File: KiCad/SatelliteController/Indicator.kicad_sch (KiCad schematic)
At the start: 36 parts

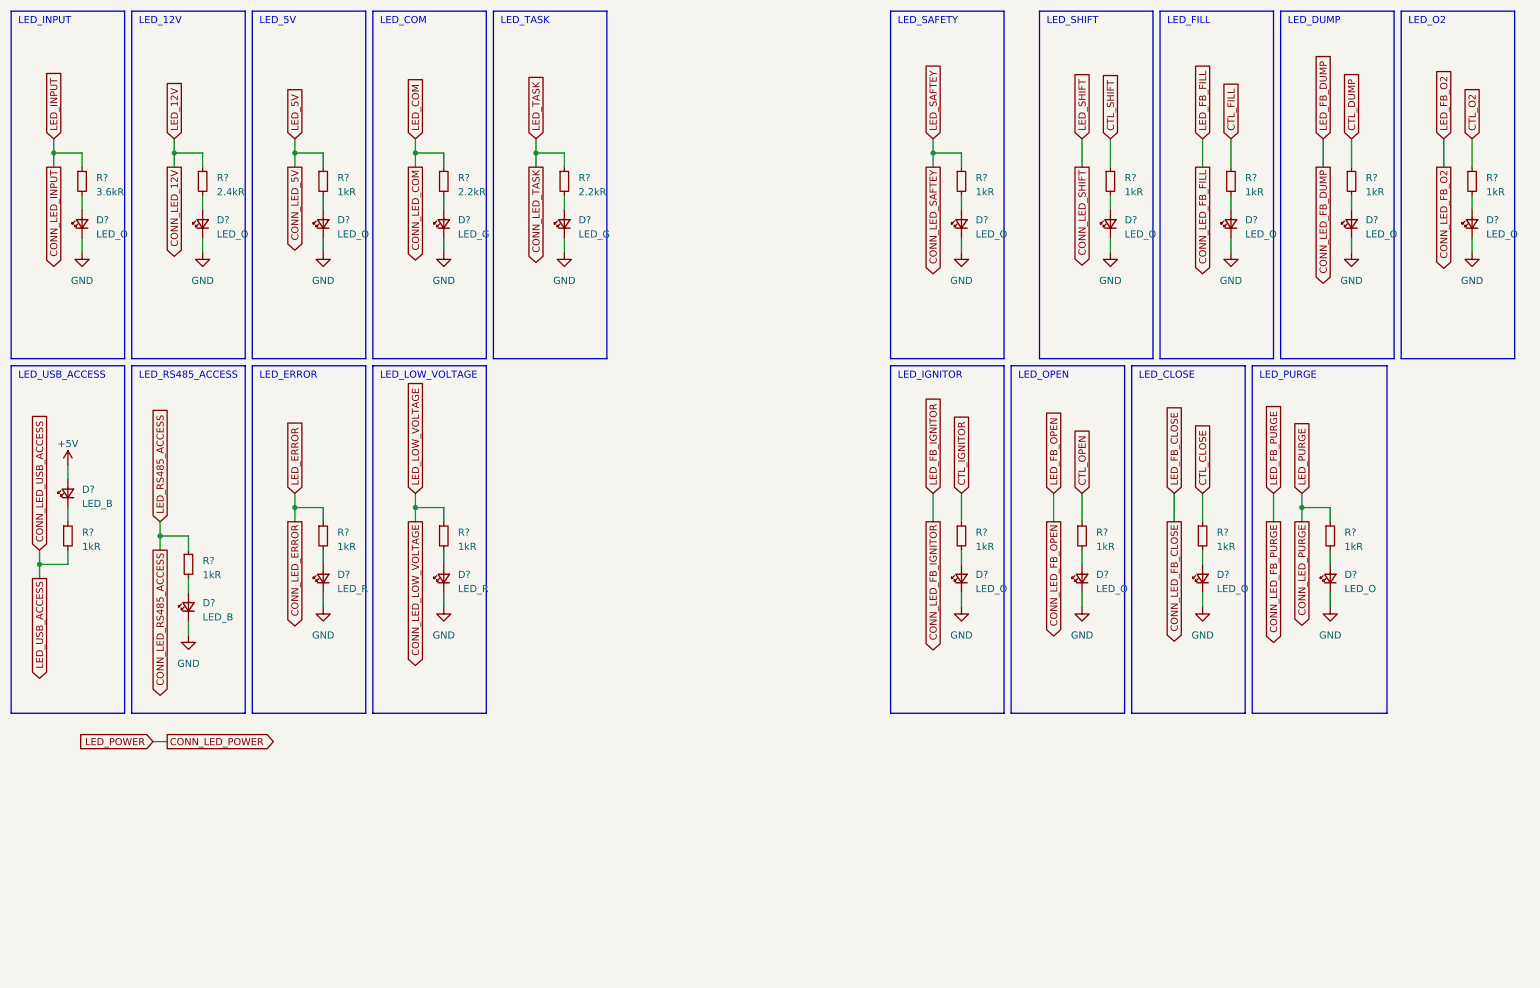
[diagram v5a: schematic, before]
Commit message: サテコンのクリスマスツリーを削除
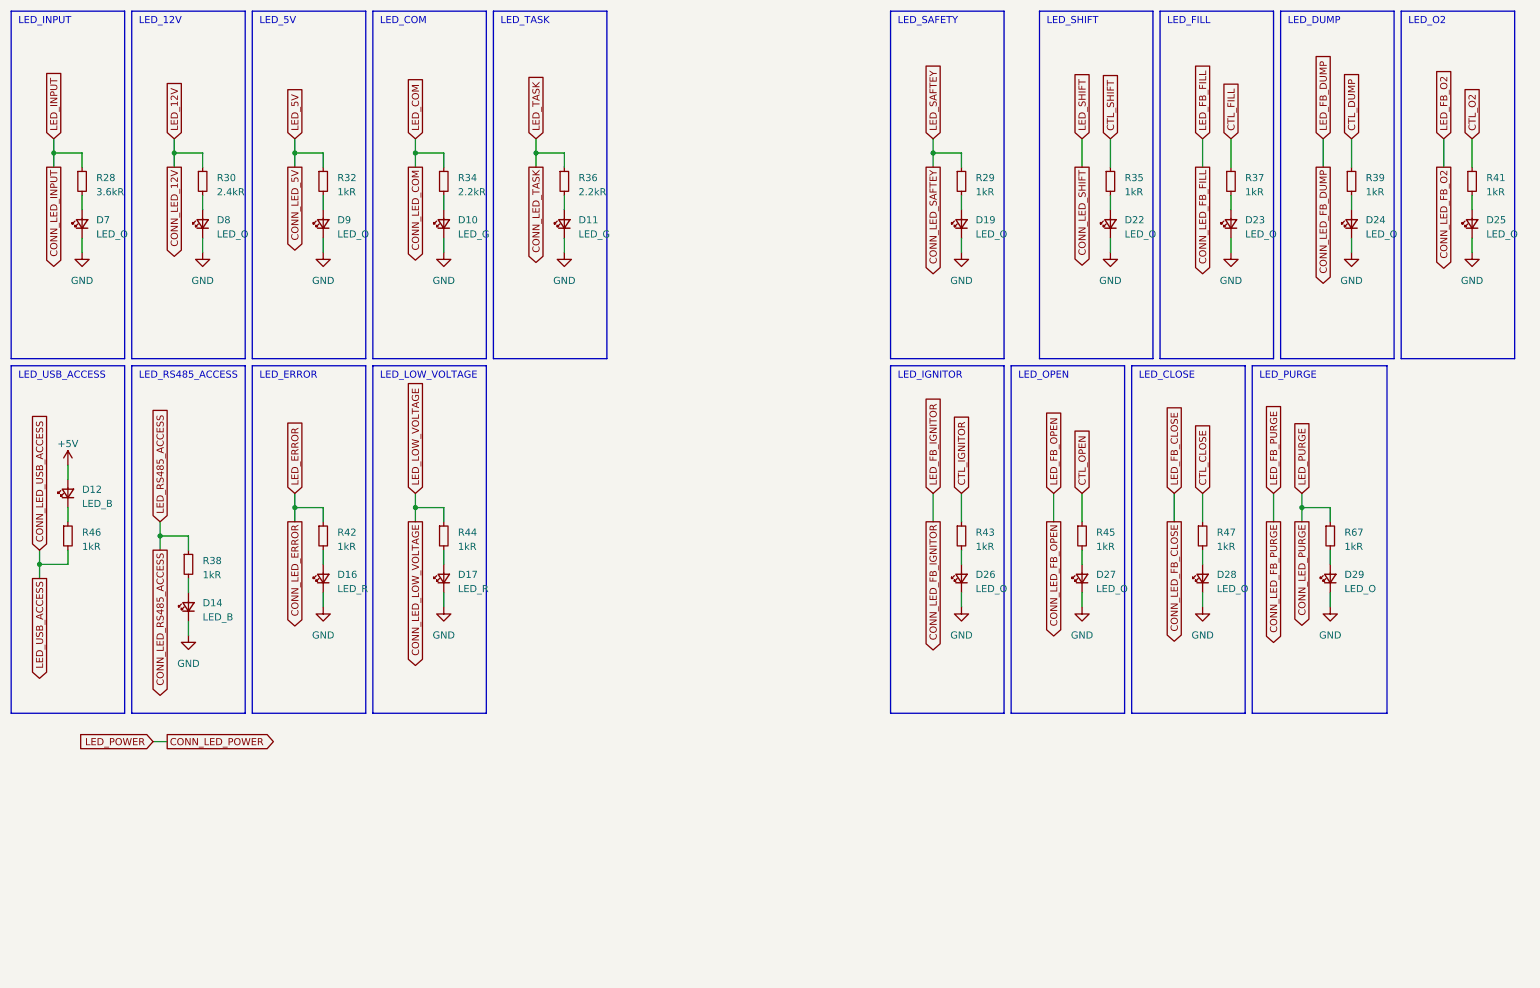
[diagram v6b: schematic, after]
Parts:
- gave numbers to parts that had none: 36

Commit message: FB_SHIFTの配線を修正
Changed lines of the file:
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@@
 		)
 	)
-	(global_label "LED_SHIFT"
+	(global_label "LED_FB_SHIFT"
 		(shape input)
 		(at 204.47 35.56 90)
@@
 		)
 		(property "Intersheetrefs" "${INTERSHEET_REFS}"
-			(at 204.47 23.0385 90)
+			(at 204.47 19.6329 90)
 			(effects
 				(font
@@
 		)
 	)
-	(global_label "CONN_LED_SHIFT"
+	(global_label "CONN_LED_FB_SHIFT"
 		(shape output)
 		(at 204.47 40.64 270)
@@
 		)
 		(property "Intersheetrefs" "${INTERSHEET_REFS}"
-			(at 204.47 59.3906 90)
+			(at 204.47 62.7962 90)
 			(effects
 				(font

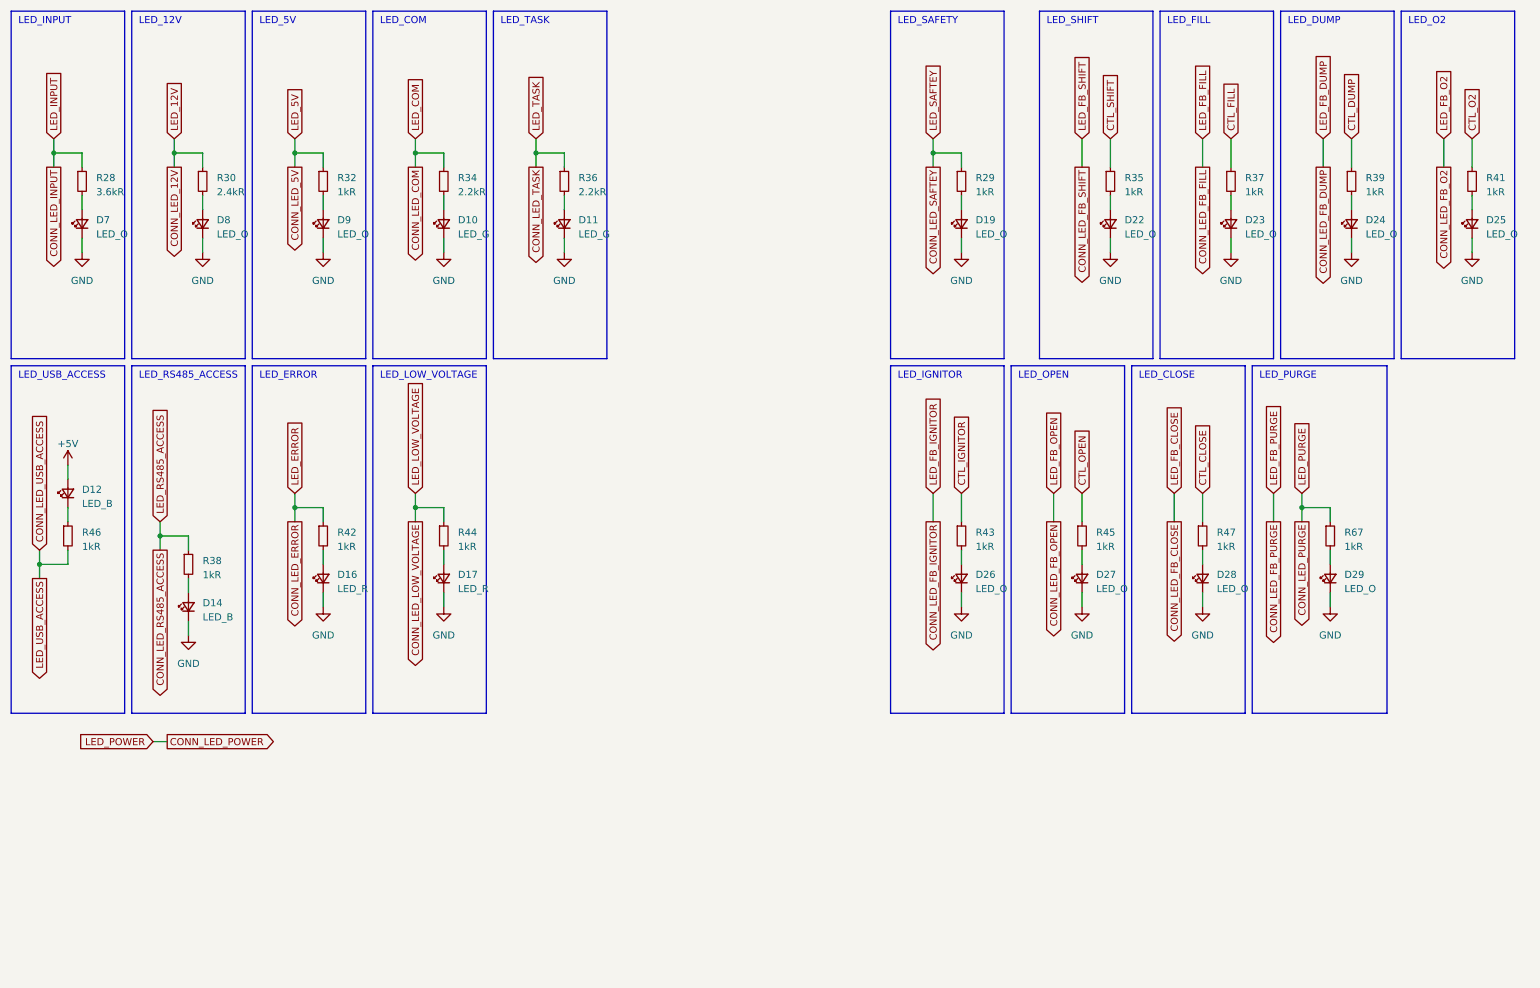
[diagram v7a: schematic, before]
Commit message: 電磁弁制御回路を整理
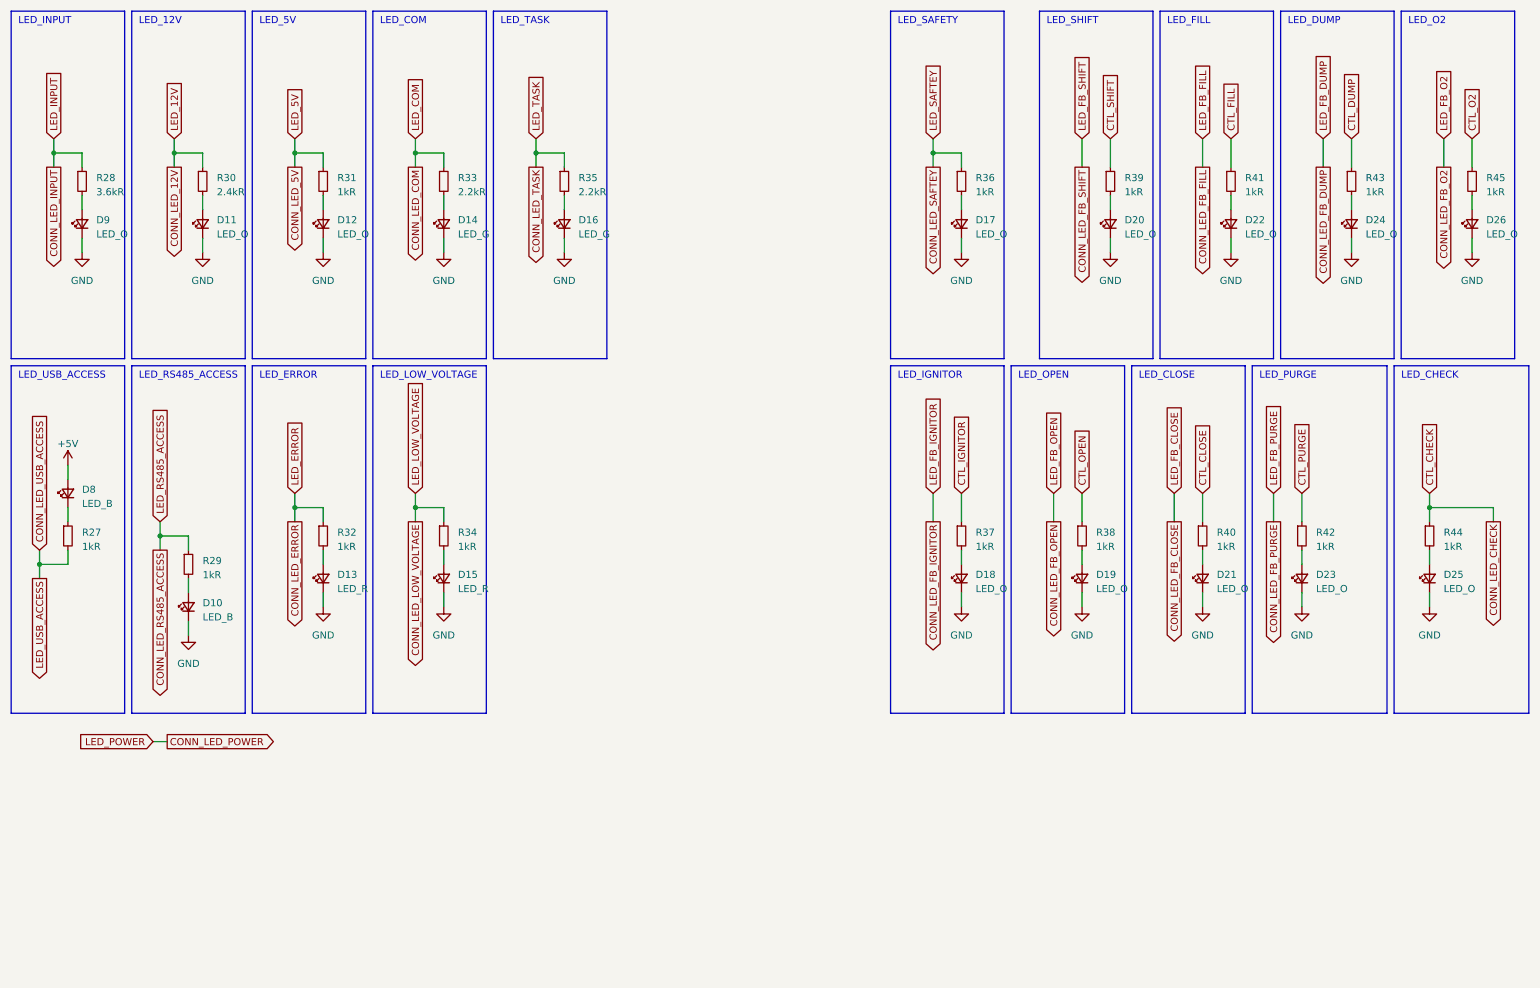
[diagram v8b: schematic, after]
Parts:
- added D25: LED_O, LED_SMD:LED_0603_1608Metric_Pad1.05x0.95mm_HandSolder, symbol Device:LED_Small
- added R44: 1kR, Resistor_SMD:R_0603_1608Metric_Pad0.98x0.95mm_HandSolder, symbol Device:R_Small
- renumbered D14 to D10, D8 to D11, D9 to D12, D16 to D13, D10 to D14, D17 to D15, D11 to D16, D19 to D17, D26 to D18, D27 to D19, D22 to D20, D28 to D21, D23 to D22, D29 to D23, D25 to D26, D12 to D8, D7 to D9, R46 to R27, R38 to R29, R32 to R31, R42 to R32, R34 to R33, R44 to R34, R36 to R35, R29 to R36, R43 to R37, R45 to R38, R35 to R39, R47 to R40, R37 to R41, R67 to R42, R39 to R43, R41 to R45
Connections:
- net GND: now also D25.1 (K)
- net CONN_LED_PURGE renamed CTL_PURGE
- new net: D25.2 (A), R44.2
- new net CONN_LED_CHECK: R44.1
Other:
- note added: "LED_CHECK"
- moved on the sheet: D23, R42
